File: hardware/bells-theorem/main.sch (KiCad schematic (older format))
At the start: 10 parts, among them J2 left, J3 right, U1 Teensy4.1, U4 PI4MSD5V9540B

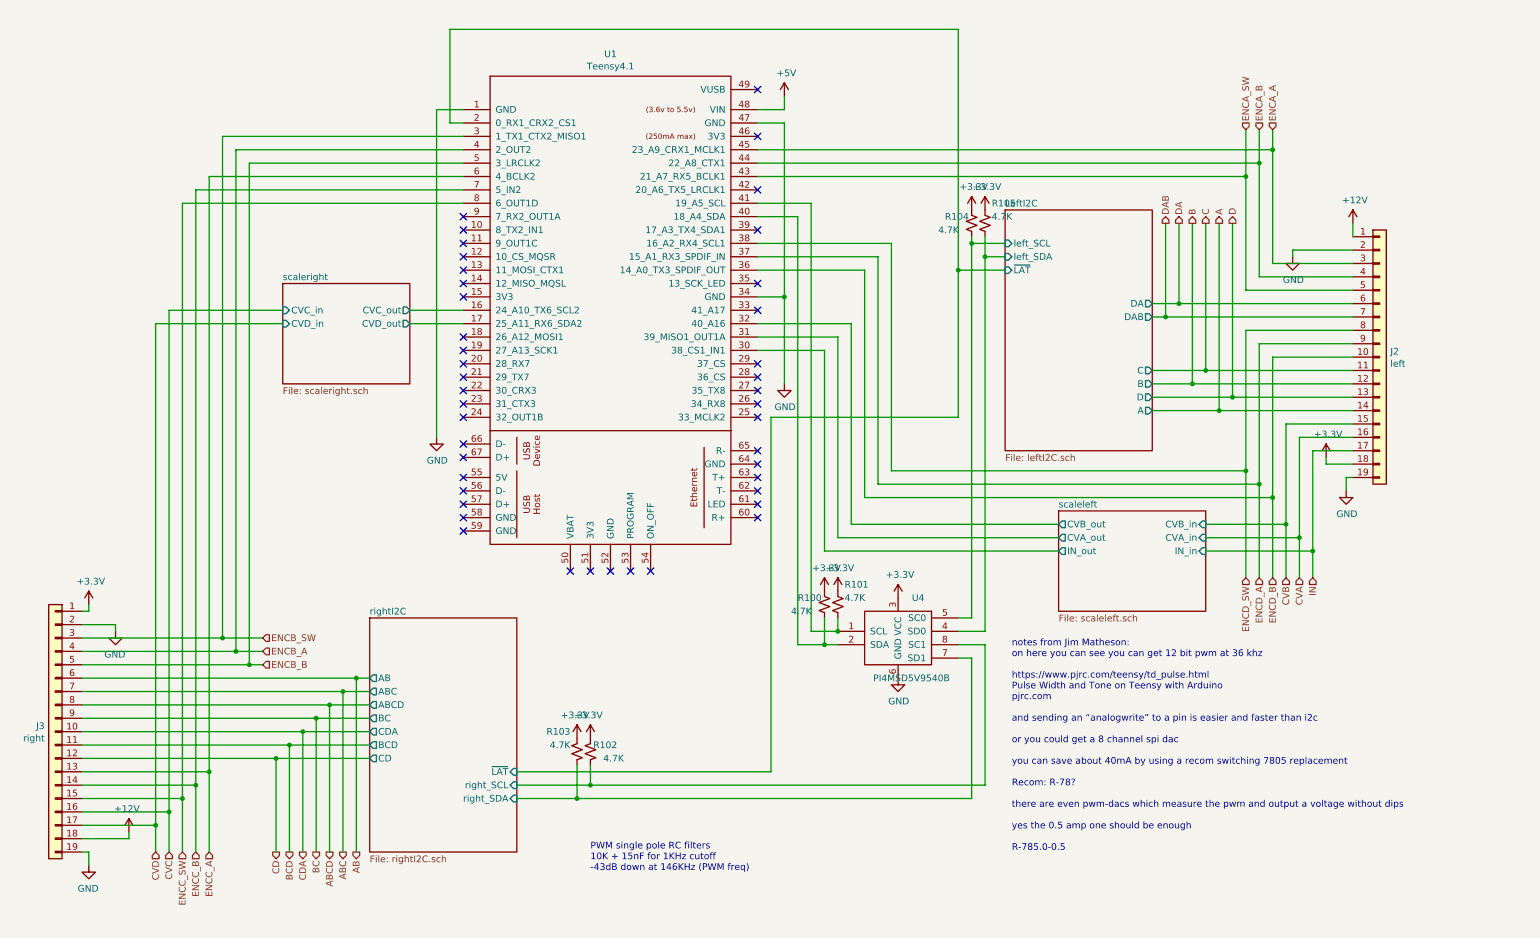
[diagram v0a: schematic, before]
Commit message: take gerbers out of the repo, push latest updates
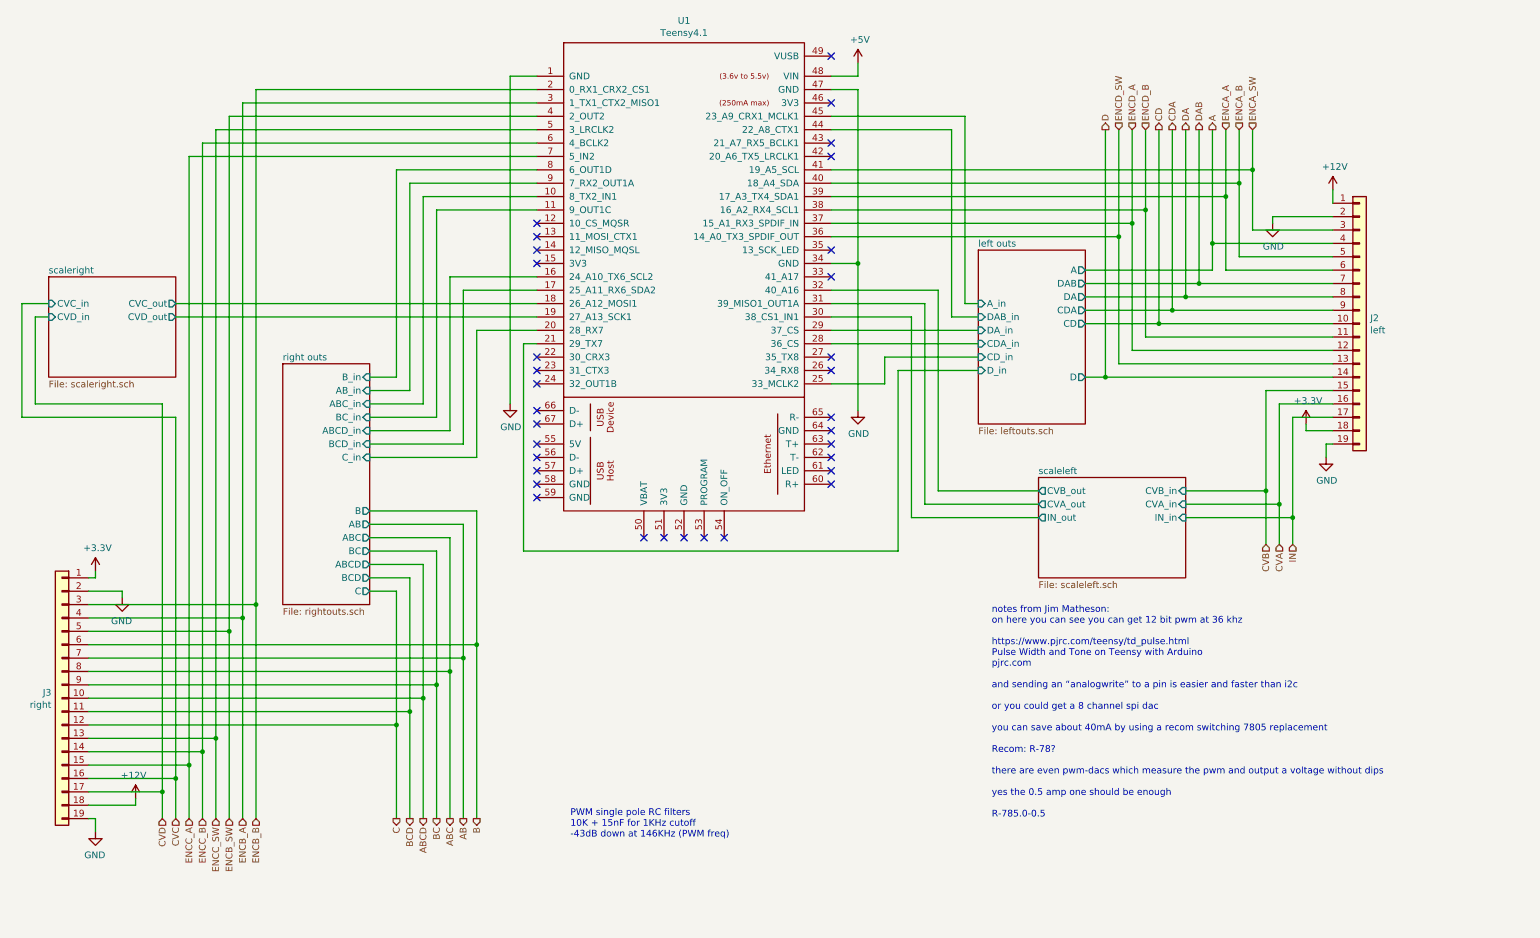
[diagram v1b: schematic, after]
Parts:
- removed R100, R101, R102, R103, R104, R105: 4.7K, Resistor_SMD:R_0805_2012Metric_Pad1.15x1.40mm_HandSolder, symbol device:R_Small_US
- removed U4: PI4MSD5V9540B, Package_SO:MSOP-8_3x3mm_P0.65mm, symbol petelib:PI4MSD5V9540B
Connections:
- net LeftI2C/~LAT is gone; now on net ENCB_B: U1.2 (0_RX1_CRX2_CS1)
- net A: now also J2.4 (Pin_4); no longer J2.14 (Pin_14)
- net AB: now also J3.7 (Pin_7); no longer J3.6 (Pin_6)
- net ABC: now also J3.8 (Pin_8); no longer J3.7 (Pin_7)
- net ABCD: now also J3.10 (Pin_10); no longer J3.8 (Pin_8)
- net B: now also J3.6 (Pin_6); no longer J2.12 (Pin_12)
- net C: now also J3.12 (Pin_12); no longer J2.11 (Pin_11)
- net CD: now also J2.10 (Pin_10); no longer J3.12 (Pin_12)
- net CDA: now also J2.9 (Pin_9); no longer J3.10 (Pin_10)
- net D: now also J2.14 (Pin_14); no longer J2.13 (Pin_13)
- net DA: now also J2.8 (Pin_8); no longer J2.6 (Pin_6)
- net ENCA_A: now also J2.6 (Pin_6), U1.39 (17_A3_TX4_SDA1); no longer J2.3 (Pin_3), U1.45 (23_A9_CRX1_MCLK1)
- net ENCA_B: now also J2.5 (Pin_5), U1.40 (18_A4_SDA); no longer J2.4 (Pin_4), U1.44 (22_A8_CTX1)
- net ENCA_SW: now also J2.3 (Pin_3), U1.41 (19_A5_SCL); no longer J2.5 (Pin_5), U1.43 (21_A7_RX5_BCLK1)
- net ENCB_A: now also U1.3 (1_TX1_CTX2_MISO1); no longer U1.4 (2_OUT2)
- net ENCB_B: now also J3.3 (Pin_3); no longer J3.5 (Pin_5), U1.5 (3_LRCLK2)
- net ENCB_SW: now also J3.5 (Pin_5), U1.4 (2_OUT2); no longer J3.3 (Pin_3), U1.3 (1_TX1_CTX2_MISO1)
- net ENCC_A: now also J3.15 (Pin_15), U1.7 (5_IN2); no longer J3.13 (Pin_13), U1.6 (4_BCLK2)
- net ENCC_B: now also U1.6 (4_BCLK2); no longer U1.7 (5_IN2)
- net ENCC_SW: now also J3.13 (Pin_13), U1.5 (3_LRCLK2); no longer J3.15 (Pin_15), U1.8 (6_OUT1D)
- net ENCD_A: now also J2.12 (Pin_12); no longer J2.9 (Pin_9)
- net ENCD_B: now also J2.11 (Pin_11), U1.38 (16_A2_RX4_SCL1); no longer J2.10 (Pin_10), U1.36 (14_A0_TX3_SPDIF_OUT)
- net ENCD_SW: now also J2.13 (Pin_13), U1.36 (14_A0_TX3_SPDIF_OUT); no longer J2.8 (Pin_8), U1.38 (16_A2_RX4_SCL1)
- net scaleright/CVC_out: now also U1.18 (26_A12_MOSI1); no longer U1.16 (24_A10_TX6_SCL2)
- net scaleright/CVD_out: now also U1.19 (27_A13_SCK1); no longer U1.17 (25_A11_RX6_SDA2)
- net right outs/ABC_in: now reaches U1.10 (8_TX2_IN1)
- net right outs/BC_in: now reaches U1.11 (9_OUT1C)
- net right outs/C_in: now reaches U1.20 (28_RX7)
- net left outs/D_in: now reaches U1.21 (29_TX7)
- net left outs/CD_in: now reaches U1.25 (33_MCLK2)
- net left outs/CDA_in: now reaches U1.28 (36_CS)
- net left outs/DA_in: now reaches U1.29 (37_CS)
- net right outs/AB_in: now reaches U1.9 (7_RX2_OUT1A)
- new net left outs/A_in: U1.45 (23_A9_CRX1_MCLK1)
- new net left outs/DAB_in: U1.44 (22_A8_CTX1)
- new net right outs/ABCD_in: U1.16 (24_A10_TX6_SCL2)
- new net right outs/BCD_in: U1.17 (25_A11_RX6_SDA2)
- new net right outs/B_in: U1.8 (6_OUT1D)
- no-connect marks 43 -> 33
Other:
- moved on the sheet: J2, J3, U1

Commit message: version 0.3, update for corrected LED drivers, other tweaks
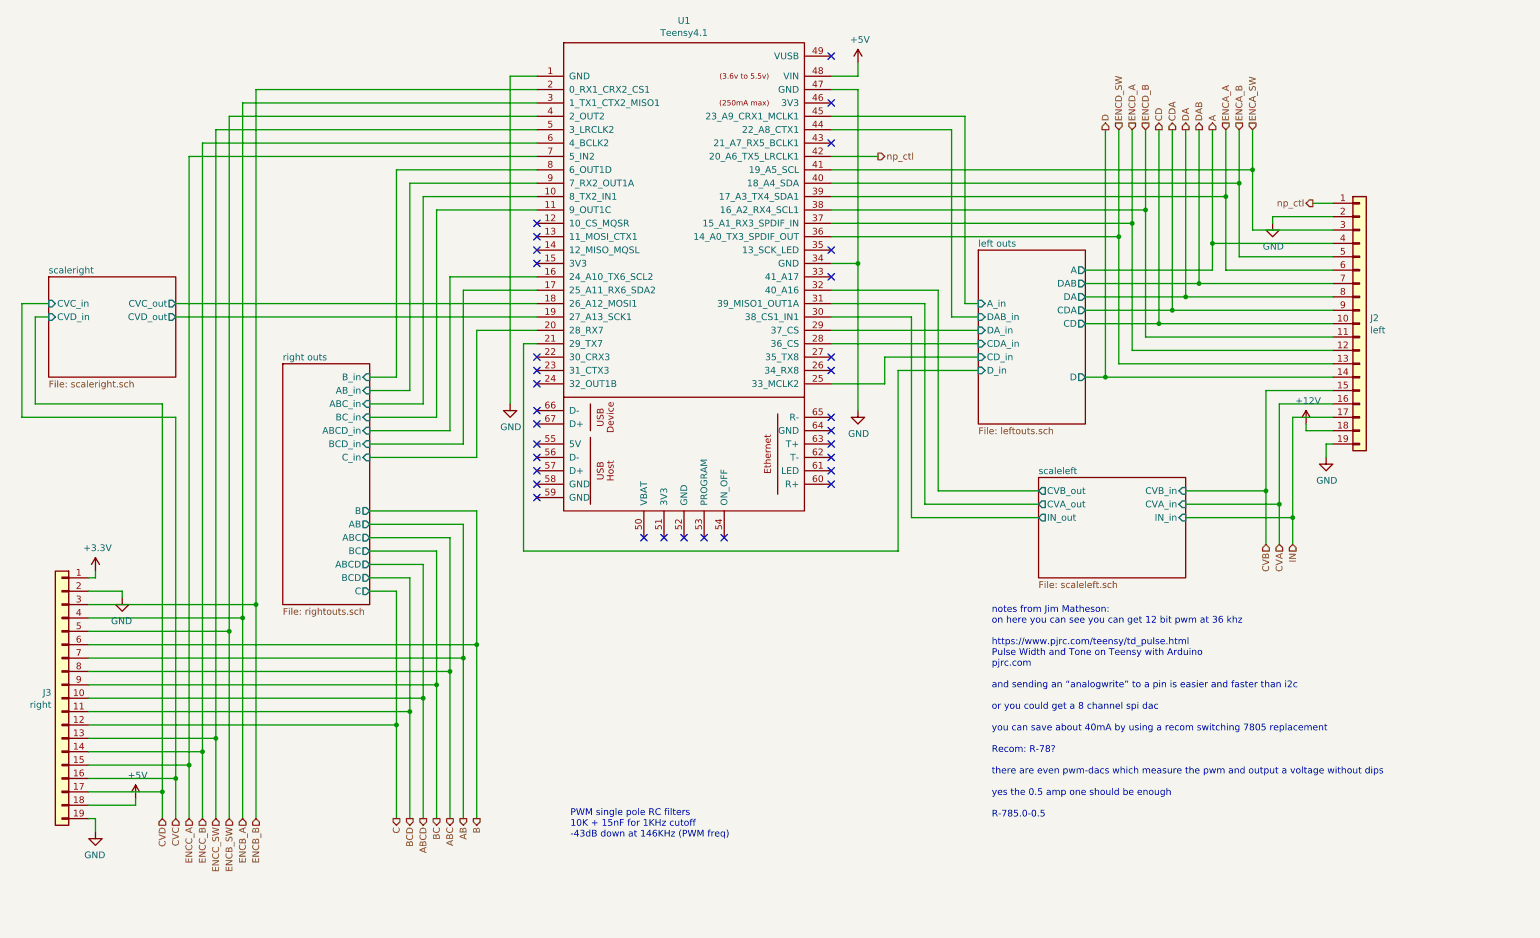
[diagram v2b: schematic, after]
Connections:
- net +12V: now also J2.18 (Pin_18); no longer J2.1 (Pin_1), J3.18 (Pin_18)
- net +3V3: no longer J2.18 (Pin_18)
- net +5V: now also J3.18 (Pin_18)
- net np_ctl: now reaches U1.42 (20_A6_TX5_LRCLK1)
- net np_ctl: now also J2.1 (Pin_1)
- no-connect marks 33 -> 32
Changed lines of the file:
@@
 	4600 3000 4500 3000
 NoConn ~ 6800 2300
-NoConn ~ 6800 1600
 NoConn ~ 6800 1500
 NoConn ~ 6800 1200
@@
 Text HLabel 3850 6550 3    50   Output ~ 0
 BC
-$Comp
-L power:+3.3V #PWR0199
-U 1 1 5FA79550
-P 1300 4700
-F 0 "#PWR0199" H 1300 4550 50  0001 C CNN
-F 1 "+3.3V" H 1315 4873 50  0000 C CNN
-F 2 "" H 1300 4700 50  0001 C CNN
-F 3 "" H 1300 4700 50  0001 C CNN
-	1    1300 4700
-	1    0    0    -1
-$EndComp
-$Comp
-L power:+3.3V #PWR0198
-U 1 1 5FA78B95
-P 10350 3600
-F 0 "#PWR0198" H 10350 3450 50  0001 C CNN
-F 1 "+3.3V" H 10365 3773 50  0000 C CNN
-F 2 "" H 10350 3600 50  0001 C CNN
-F 3 "" H 10350 3600 50  0001 C CNN
-	1    10350 3600
-	1    0    0    -1
-$EndComp
 Wire Wire Line
 	10250 3550 10550 3550
@@
 Text HLabel 3550 6550 3    50   Output ~ 0
 C
-Wire Wire Line
-	10550 1850 10550 1950
 Wire Wire Line
 	1250 6250 1900 6250
@@
 Wire Wire Line
 	1300 4700 1300 4750
-$Comp
-L power:+12V #PWR?
-U 1 1 5F8674B5
-P 1600 6400
-AR Path="/5F7954A8/5F8674B5" Ref="#PWR?"  Part="1"
-AR Path="/5CEF66AD/5F8674B5" Ref="#PWR056"  Part="1"
-F 0 "#PWR056" H 1600 6250 50  0001 C CNN
-F 1 "+12V" H 1615 6573 50  0000 C CNN
-F 2 "" H 1600 6400 50  0001 C CNN
-F 3 "" H 1600 6400 50  0001 C CNN
-	1    1600 6400
-	-1   0    0    -1
-$EndComp
 $Comp
 L power:GND #PWR?
@@
 ENCD_A
 $Comp
-L power:+12V #PWR?
-U 1 1 5F97FD02
-P 10550 1850
-AR Path="/5F7954A8/5F97FD02" Ref="#PWR?"  Part="1"
-AR Path="/5CEF66AD/5F97FD02" Ref="#PWR05"  Part="1"
-F 0 "#PWR05" H 10550 1700 50  0001 C CNN
-F 1 "+12V" H 10565 2023 50  0000 C CNN
-F 2 "" H 10550 1850 50  0001 C CNN
-F 3 "" H 10550 1850 50  0001 C CNN
-	1    10550 1850
-	1    0    0    -1
-$EndComp
-$Comp
 L power:GND #PWR?
 U 1 1 5F97FCF6
@@
 Wire Wire Line
 	2300 1300 2300 5150
+$Comp
+L power:+12V #PWR?
+U 1 1 5F97FD02
+P 10350 3600
+AR Path="/5F7954A8/5F97FD02" Ref="#PWR?"  Part="1"
+AR Path="/5CEF66AD/5F97FD02" Ref="#PWR05"  Part="1"
+F 0 "#PWR05" H 10350 3450 50  0001 C CNN
+F 1 "+12V" H 10365 3773 50  0000 C CNN
+F 2 "" H 10350 3600 50  0001 C CNN
+F 3 "" H 10350 3600 50  0001 C CNN
+	1    10350 3600
+	1    0    0    -1
+$EndComp
+$Comp
+L power:+3.3V #PWR040
+U 1 1 60787F95
+P 1300 4700
+F 0 "#PWR040" H 1300 4550 50  0001 C CNN
+F 1 "+3.3V" H 1315 4873 50  0000 C CNN
+F 2 "" H 1300 4700 50  0001 C CNN
+F 3 "" H 1300 4700 50  0001 C CNN
+	1    1300 4700
+	1    0    0    -1
+$EndComp
+$Comp
+L power:+5V #PWR039
+U 1 1 60788A4D
+P 1600 6400
+F 0 "#PWR039" H 1600 6250 50  0001 C CNN
+F 1 "+5V" H 1615 6573 50  0000 C CNN
+F 2 "" H 1600 6400 50  0001 C CNN
+F 3 "" H 1600 6400 50  0001 C CNN
+	1    1600 6400
+	1    0    0    -1
+$EndComp
+Text HLabel 10400 1950 0    50   Output ~ 0
+np_ctl
+Wire Wire Line
+	10400 1950 10550 1950
+Text HLabel 7150 1600 2    50   Output ~ 0
+np_ctl
+Wire Wire Line
+	6800 1600 7150 1600
 $EndSCHEMATC

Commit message: updated for NeoPixels
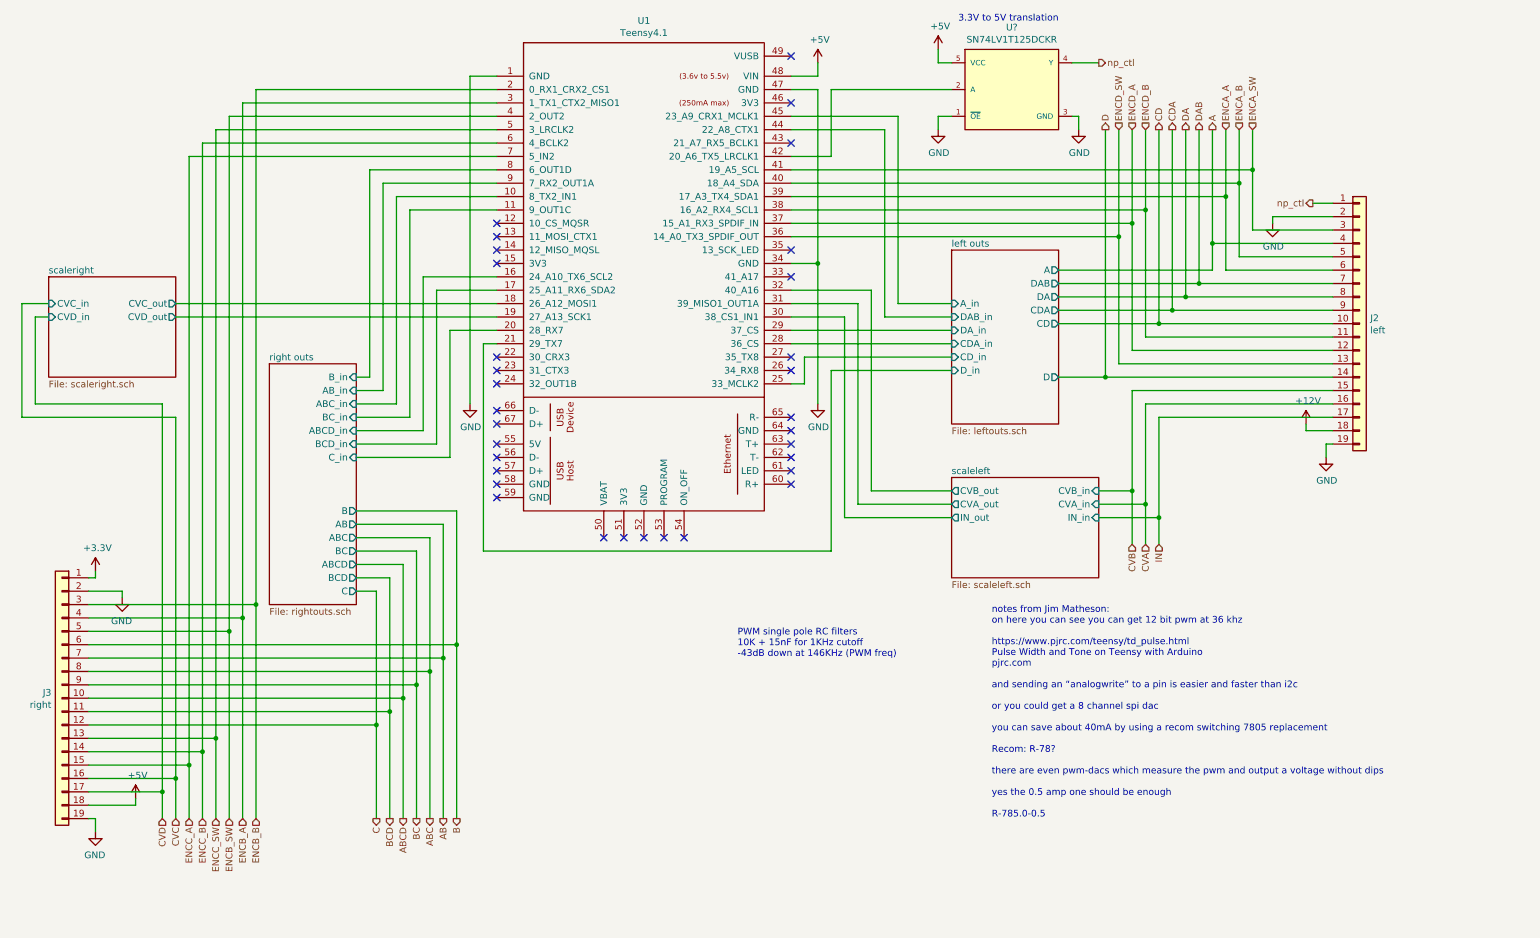
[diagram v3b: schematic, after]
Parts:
- added U?: SN74LV1T125DCKR, Texas_Instruments-DCK0005A-0-0-*, symbol EEC_lib:SN74LV1T125DCKR
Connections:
- net +5V: now also U?.5 (VCC)
- net GND: now also U?.1 (~OE~), U?.3 (GND)
- net np_ctl: now also U?.4 (Y); no longer U1.42 (20_A6_TX5_LRCLK1)
- new net: U1.42 (20_A6_TX5_LRCLK1), U?.2 (A)
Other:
- note added: "3.3V to 5V translation"
- moved on the sheet: U1
